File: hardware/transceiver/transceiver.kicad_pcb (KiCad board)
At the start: 4 copper layers, 30 x 30 mm, 50 parts, among them J1 Conn_01x04, J2 Conn_01x02, J3 Conn_Coaxial, J4 Conn_01x02, U1 SX1262IMLTRT, U2 AP2112K-3.3, U3 PE4259, U4 STM32U585CIUx, Y1 32MHz, Y2 Q13FC13500004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

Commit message: rewrote firmware
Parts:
- moved Y3 0.29 mm to (142.7, 105.8)
- moved C22 0.29 mm to (140.3, 104.9)
- moved C25 0.29 mm to (144.9, 106.7)
- moved C24 0.29 mm to (145.0, 104.4)
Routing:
- net GND: track 65.5 -> 65.6 mm, vias 133 -> 132

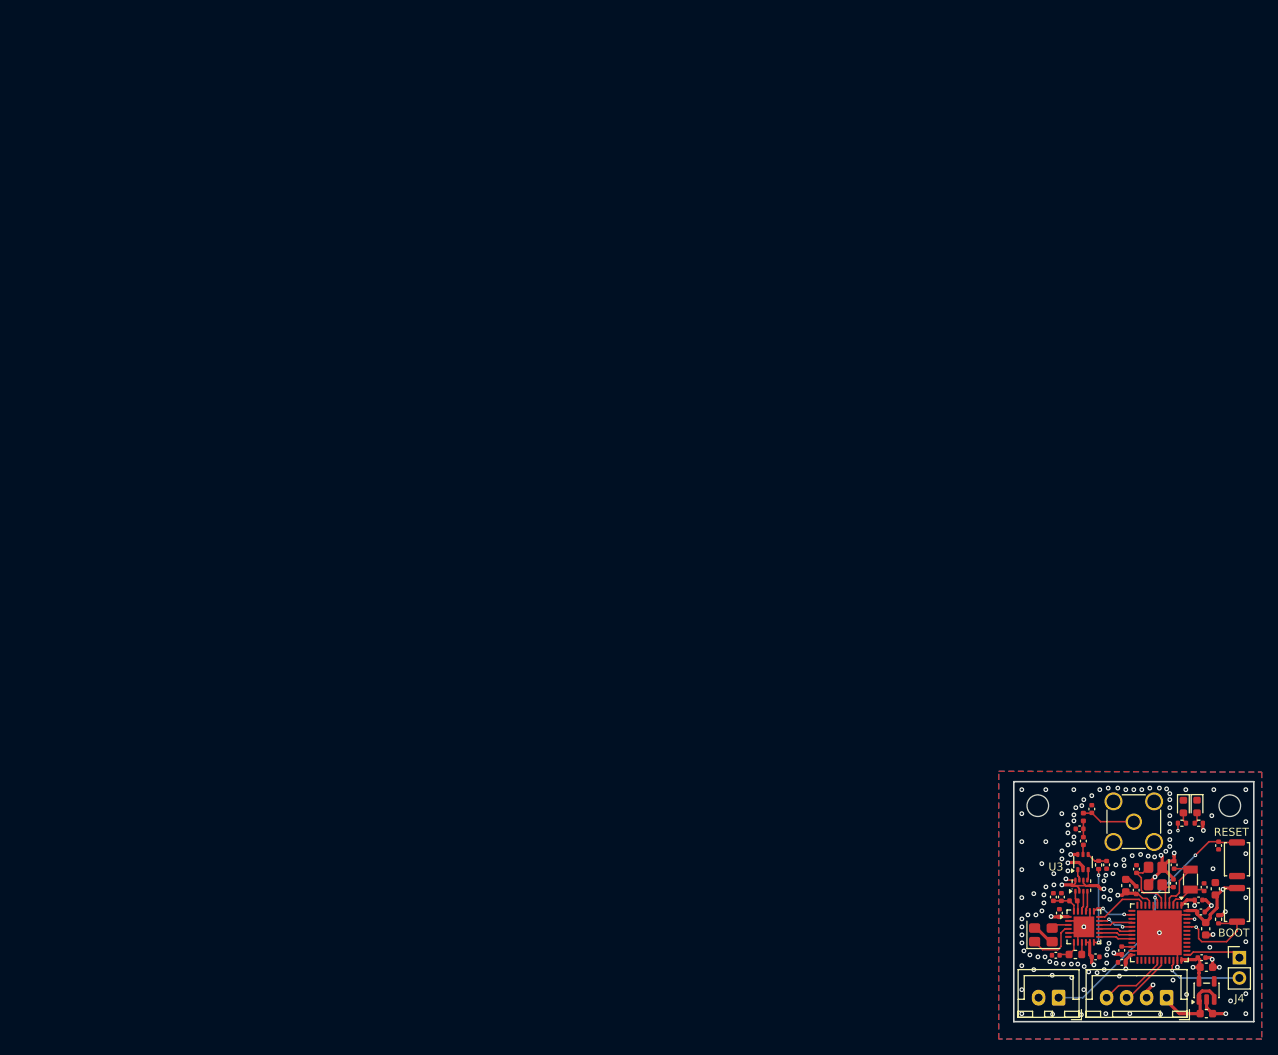
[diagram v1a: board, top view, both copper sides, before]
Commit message: updated to kicad 10
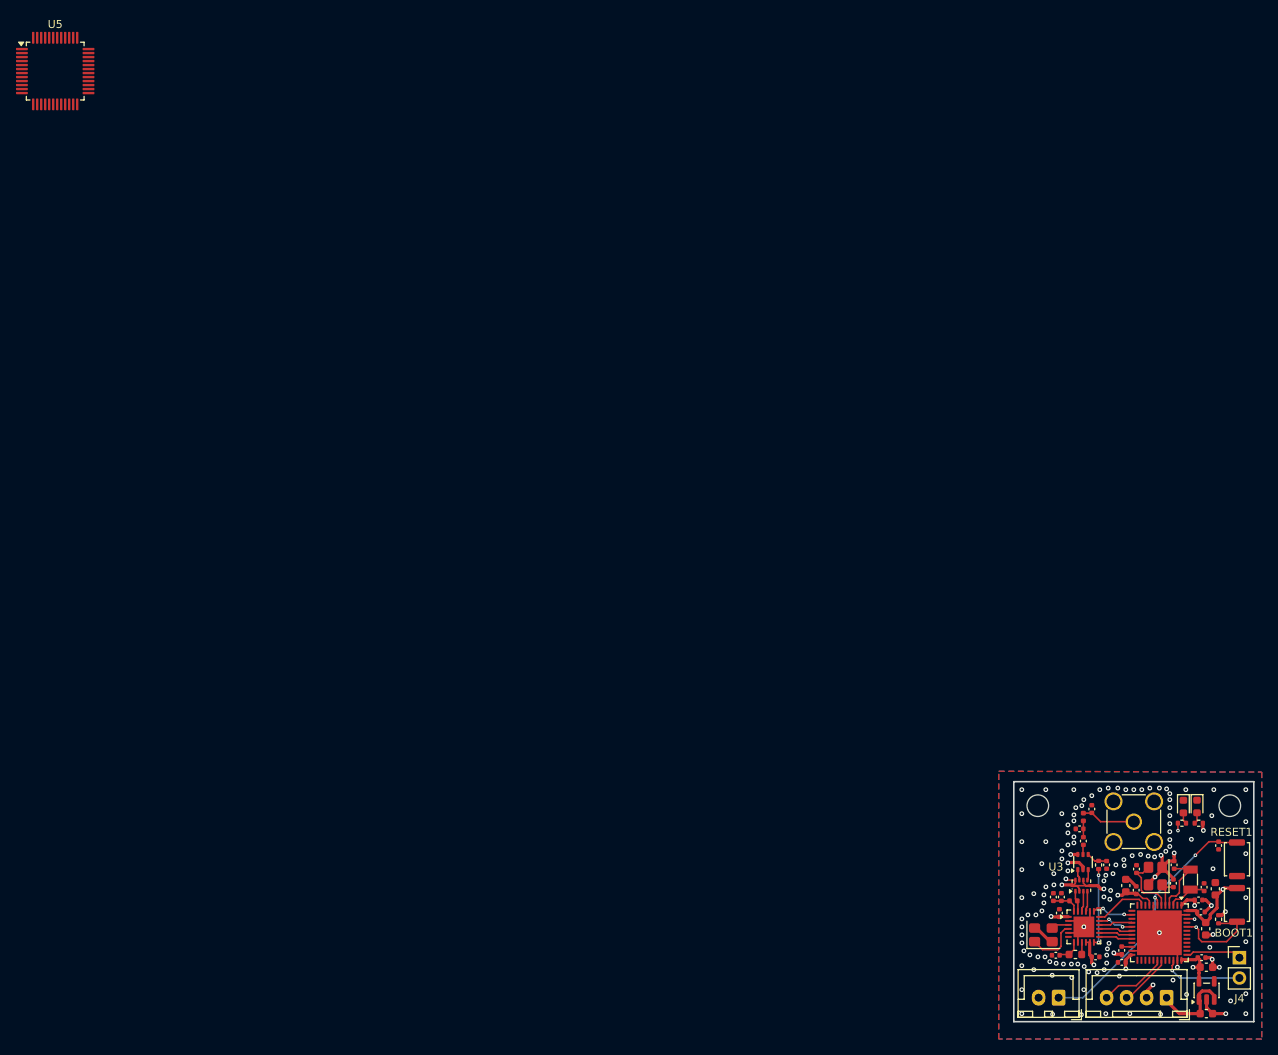
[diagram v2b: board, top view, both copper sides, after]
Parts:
- added U5: STM32U585CITx, Package_QFP:LQFP-48_7x7mm_P0.5mm, F.Cu at (5.17, 5.17)
- renumbered BOOT to BOOT1, RESET to RESET1
